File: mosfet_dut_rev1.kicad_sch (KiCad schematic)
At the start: 40 parts, among them J2 Conn, J3 Conn_01x02, J4 Conn_01x02, J5 Conn_01x02, J6 Conn_01x02, J7 USB_C_Receptacle_USB2.0_16P, Q1 AO3400A, Q2 AO3400A, Q3 AO3400A, Q4 AO3400A, U1 AP2112K-3.3, U2 USBLC6-2SC6, U4 INA219AxD, U6 ESP32-WROOM-32E, U7 CH340C

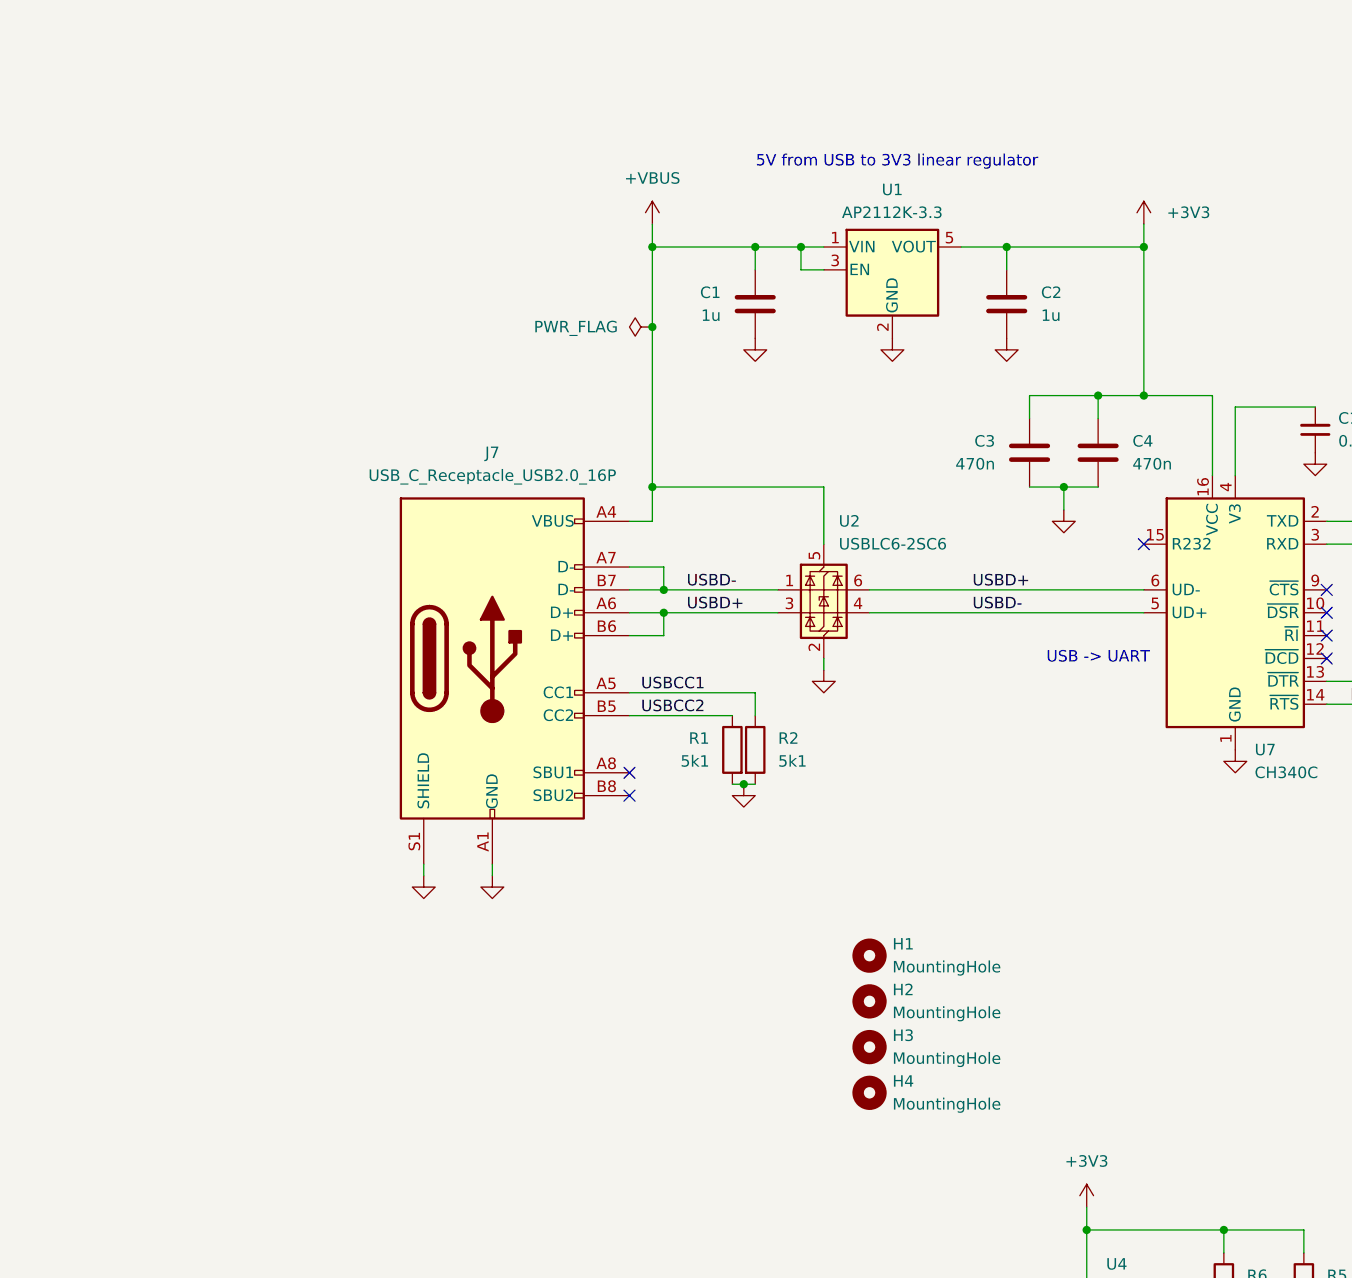
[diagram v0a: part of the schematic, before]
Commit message: Swapping to basic jlcpcb parts APK2112K-3.3 -> ME6211C33M5
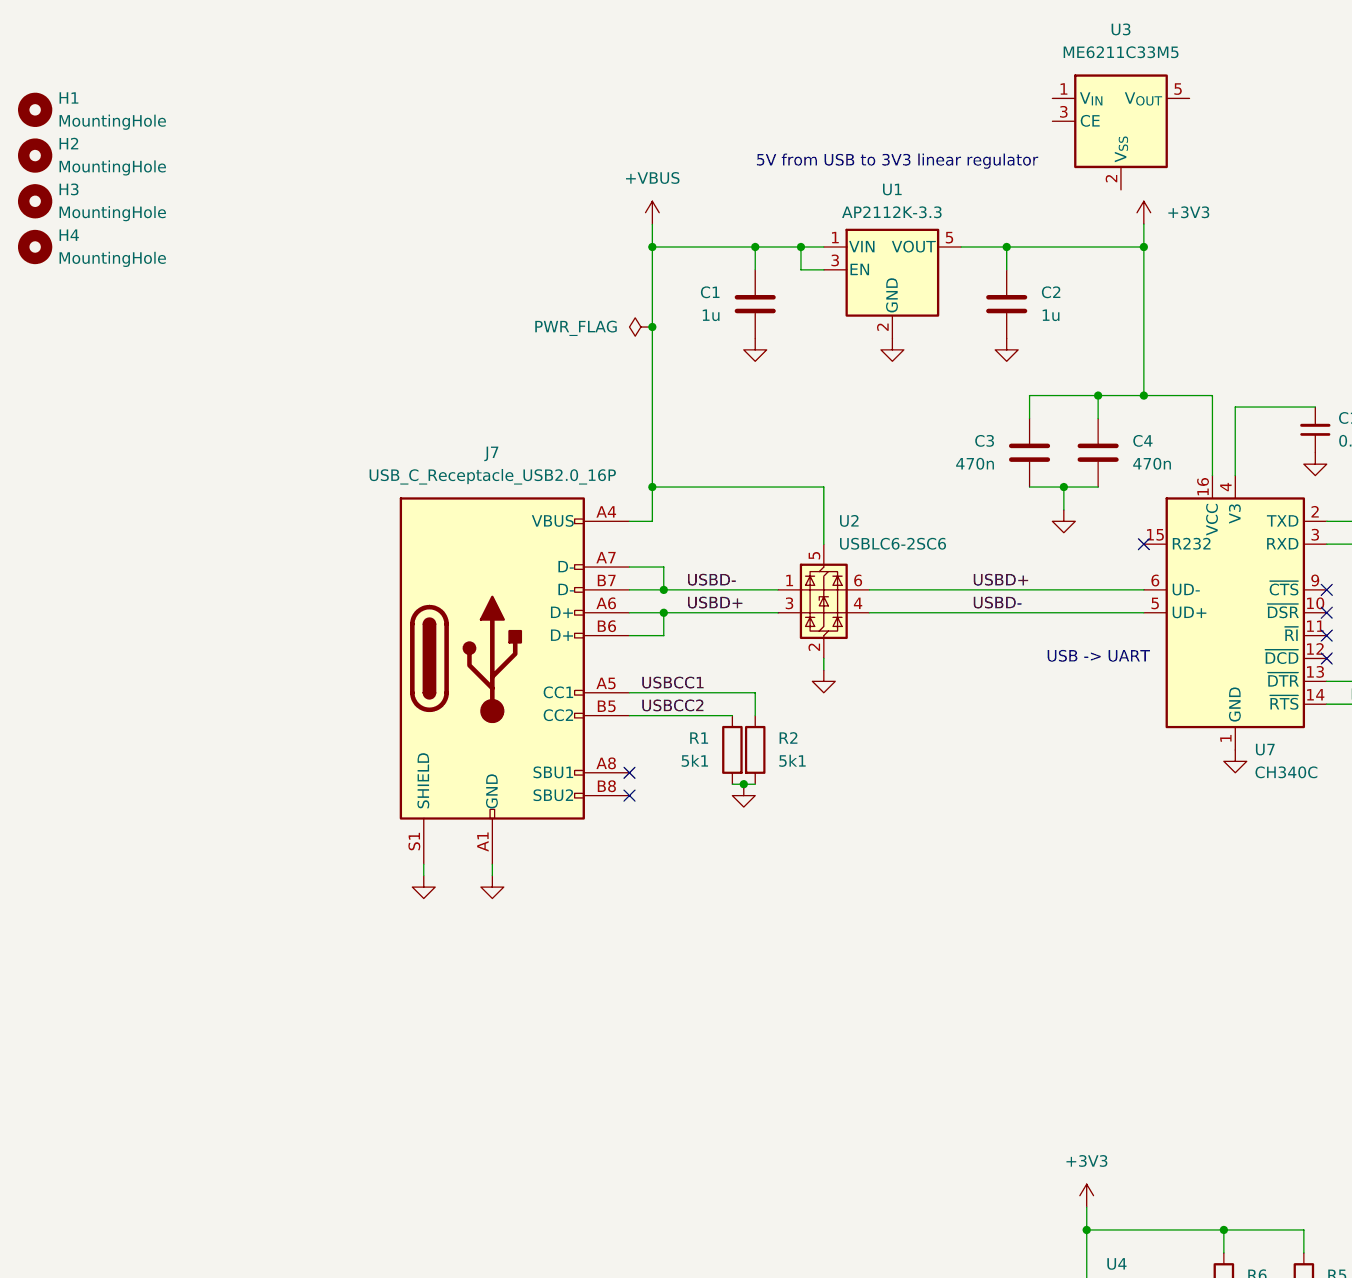
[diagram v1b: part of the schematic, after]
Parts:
- added U3: ME6211C33M5, Package_TO_SOT_SMD:SOT-23-5, symbol Regulator_Linear:ME6211C33M5
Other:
- moved on the sheet: H1, H2, H3, H4
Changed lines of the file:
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@@
 		(title "ESP32 MOSFET DUT")
 		(date "2026-01-06")
-		(rev "1.0")
+		(rev "1.1")
 		(company "Hardware Gunner")
+		(comment 1 "1.1 Swapping to basic jlcpcb parts")
+		(comment 2 "APK2112K-3.3 -> ME6211C33M5")
 	)
 	(text "I2C Addr = 0x40"
@@
 	)
 	(symbol
+		(lib_id "Regulator_Linear:ME6211C33M5")
+		(at 106.68 21.59 0)
+		(unit 1)
+		(exclude_from_sim no)
+		(in_bom yes)
+		(on_board yes)
+		(dnp no)
+		(fields_autoplaced yes)
+		(property "Reference" "U3"
+			(at 106.68 11.43 0)
+			(effects
+				(font
+					(size 1.27 1.27)
+				)
+			)
+		)
+		(property "Value" "ME6211C33M5"
+			(at 106.68 13.97 0)
+			(effects
+				(font
+					(size 1.27 1.27)
+				)
+			)
+		)
+		(property "Footprint" "Package_TO_SOT_SMD:SOT-23-5"
+			(at 106.172 35.052 0)
+			(effects
+				(font
+					(size 1.27 1.27)
+				)
+				(hide yes)
+			)
+		)
+		(property "Datasheet" "https://www.lcsc.com/datasheet/lcsc_datasheet_2304140030_MICRONE-Nanjing-Micro-One-Elec-ME6211C33R5G_C235316.pdf"
+			(at 106.934 38.608 0)
+			(effects
+				(font
+					(size 1.27 1.27)
+				)
+				(hide yes)
+			)
+		)
+		(property "Description" "500mA low dropout linear regulator, shutdown pin, 6.5V max input voltage, 3.3V fixed positive output, SOT-23-5"
+			(at 108.458 36.83 0)
+			(effects
+				(font
+					(size 1.27 1.27)
+				)
+				(hide yes)
+			)
+		)
+		(pin "4"
+		)
+		(pin "3"
+		)
+		(pin "1"
+		)
+		(pin "2"
+		)
+		(pin "5"
+		)
+		(instances
+			(project ""
+				(path "/deac0eab-811f-4736-96ff-e9a031bd3138"
+					(reference "U3")
+					(unit 1)
+				)
+			)
+		)
+	)
+	(symbol
 		(lib_id "power:+3V3")
 		(at 109.22 33.02 0)
@@
 	(symbol
 		(lib_id "Mechanical:MountingHole")
-		(at 78.74 119.38 0)
+		(at -13.97 25.4 0)
 		(unit 1)
 		(exclude_from_sim no)
@@
 		(fields_autoplaced yes)
 		(property "Reference" "H2"
-			(at 81.28 118.1099 0)
+			(at -11.43 24.1299 0)
 			(effects
 				(font
@@
 		)
 		(property "Value" "MountingHole"
-			(at 81.28 120.6499 0)
+			(at -11.43 26.6699 0)
 			(effects
 				(font
@@
 		)
 		(property "Footprint" "MountingHole:MountingHole_3.2mm_M3_Pad"
-			(at 78.74 119.38 0)
+			(at -13.97 25.4 0)
 			(effects
 				(font
@@
 		)
 		(property "Datasheet" "~"
-			(at 78.74 119.38 0)
+			(at -13.97 25.4 0)
 			(effects
 				(font
@@
 		)
 		(property "Description" "Mounting Hole without connection"
-			(at 78.74 119.38 0)
+			(at -13.97 25.4 0)
 			(effects
 				(font
@@
 	(symbol
 		(lib_id "Mechanical:MountingHole")
-		(at 78.74 114.3 0)
+		(at -13.97 20.32 0)
 		(unit 1)
 		(exclude_from_sim no)
@@
 		(fields_autoplaced yes)
 		(property "Reference" "H1"
-			(at 81.28 113.0299 0)
+			(at -11.43 19.0499 0)
 			(effects
 				(font
@@
 		)
 		(property "Value" "MountingHole"
-			(at 81.28 115.5699 0)
+			(at -11.43 21.5899 0)
 			(effects
 				(font
@@
 		)
 		(property "Footprint" "MountingHole:MountingHole_3.2mm_M3_Pad"
-			(at 78.74 114.3 0)
+			(at -13.97 20.32 0)
 			(effects
 				(font
@@
 		)
 		(property "Datasheet" "~"
-			(at 78.74 114.3 0)
+			(at -13.97 20.32 0)
 			(effects
 				(font
@@
 		)
 		(property "Description" "Mounting Hole without connection"
-			(at 78.74 114.3 0)
+			(at -13.97 20.32 0)
 			(effects
 				(font
@@
 	(symbol
 		(lib_id "Mechanical:MountingHole")
-		(at 78.74 124.46 0)
+		(at -13.97 30.48 0)
 		(unit 1)
 		(exclude_from_sim no)
@@
 		(fields_autoplaced yes)
 		(property "Reference" "H3"
-			(at 81.28 123.1899 0)
+			(at -11.43 29.2099 0)
 			(effects
 				(font
@@
 		)
 		(property "Value" "MountingHole"
-			(at 81.28 125.7299 0)
+			(at -11.43 31.7499 0)
 			(effects
 				(font
@@
 		)
 		(property "Footprint" "MountingHole:MountingHole_3.2mm_M3_Pad"
-			(at 78.74 124.46 0)
+			(at -13.97 30.48 0)
 			(effects
 				(font
@@
 		)
 		(property "Datasheet" "~"
-			(at 78.74 124.46 0)
+			(at -13.97 30.48 0)
 			(effects
 				(font
@@
 		)
 		(property "Description" "Mounting Hole without connection"
-			(at 78.74 124.46 0)
+			(at -13.97 30.48 0)
 			(effects
 				(font
@@
 	(symbol
 		(lib_id "Mechanical:MountingHole")
-		(at 78.74 129.54 0)
+		(at -13.97 35.56 0)
 		(unit 1)
 		(exclude_from_sim no)
@@
 		(fields_autoplaced yes)
 		(property "Reference" "H4"
-			(at 81.28 128.2699 0)
+			(at -11.43 34.2899 0)
 			(effects
 				(font
@@
 		)
 		(property "Value" "MountingHole"
-			(at 81.28 130.8099 0)
+			(at -11.43 36.8299 0)
 			(effects
 				(font
@@
 		)
 		(property "Footprint" "MountingHole:MountingHole_3.2mm_M3_Pad"
-			(at 78.74 129.54 0)
+			(at -13.97 35.56 0)
 			(effects
 				(font
@@
 		)
 		(property "Datasheet" "~"
-			(at 78.74 129.54 0)
+			(at -13.97 35.56 0)
 			(effects
 				(font
@@
 		)
 		(property "Description" "Mounting Hole without connection"
-			(at 78.74 129.54 0)
+			(at -13.97 35.56 0)
 			(effects
 				(font

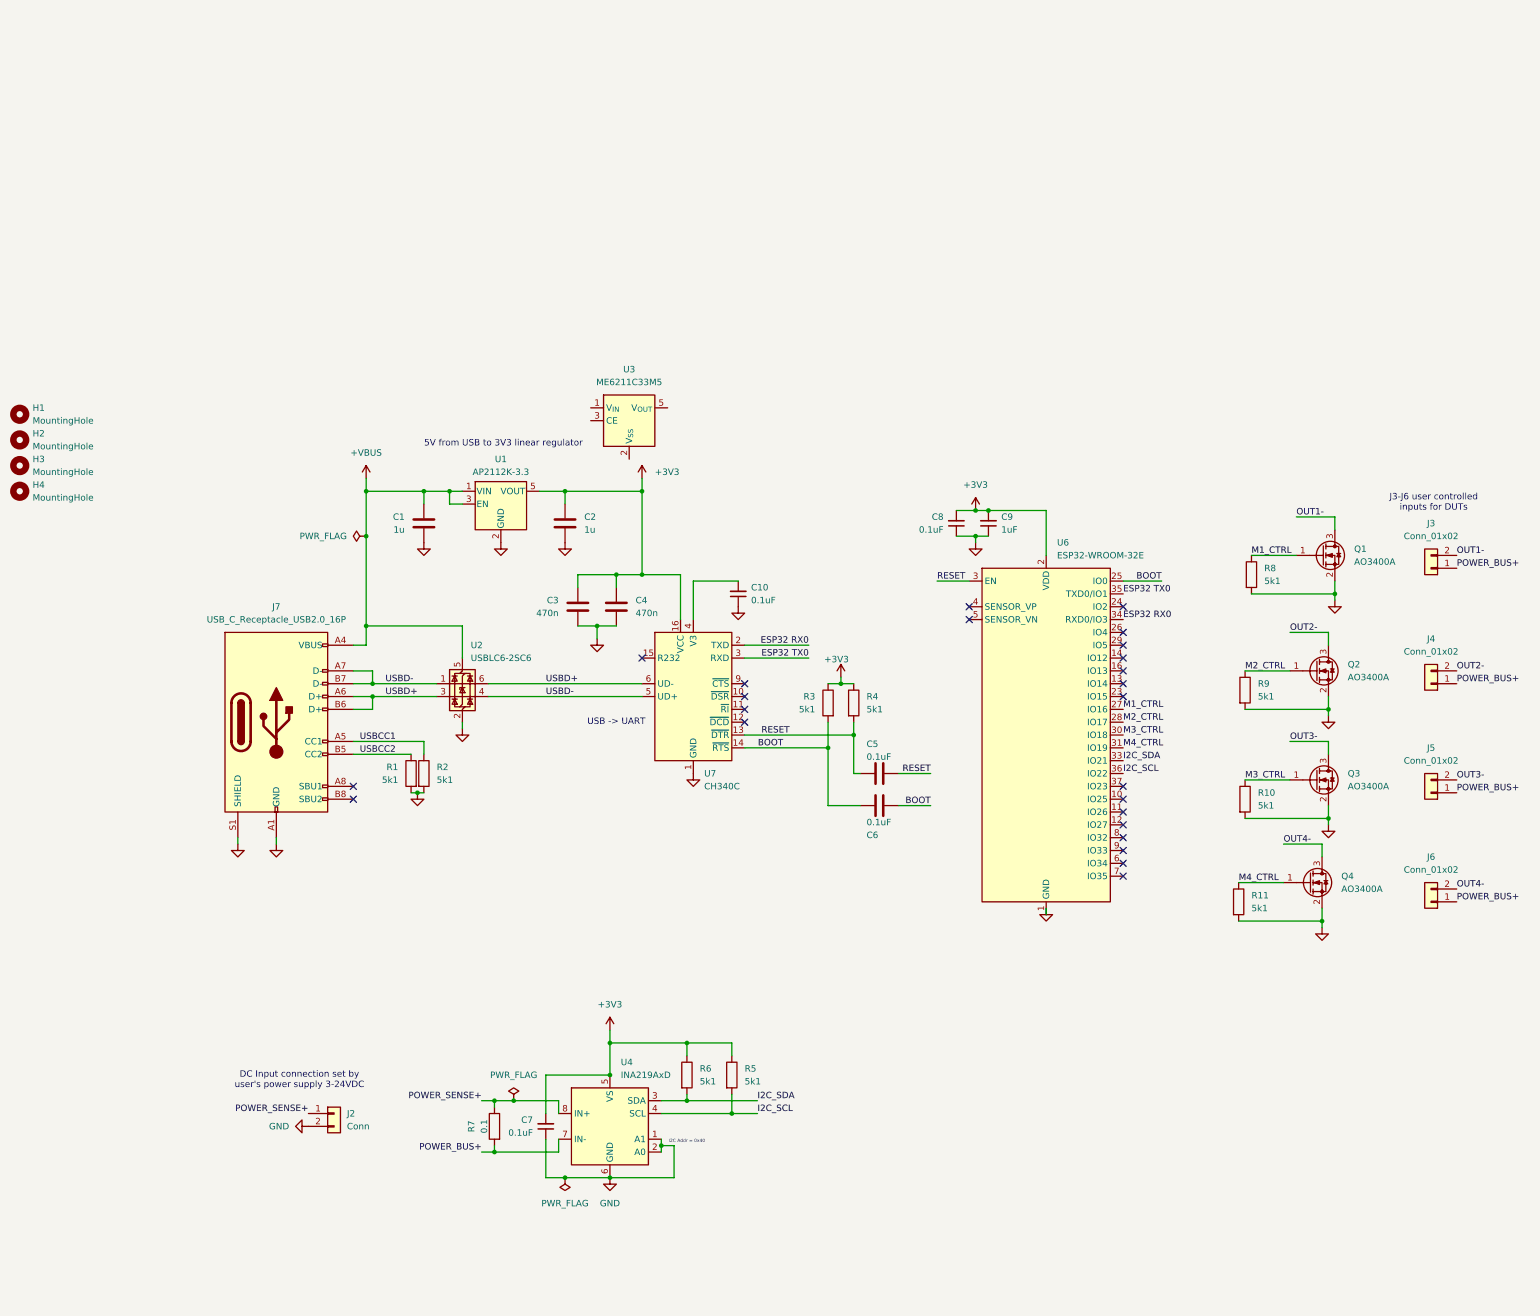
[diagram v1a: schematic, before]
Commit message: MUX/Shunts schematic wiring
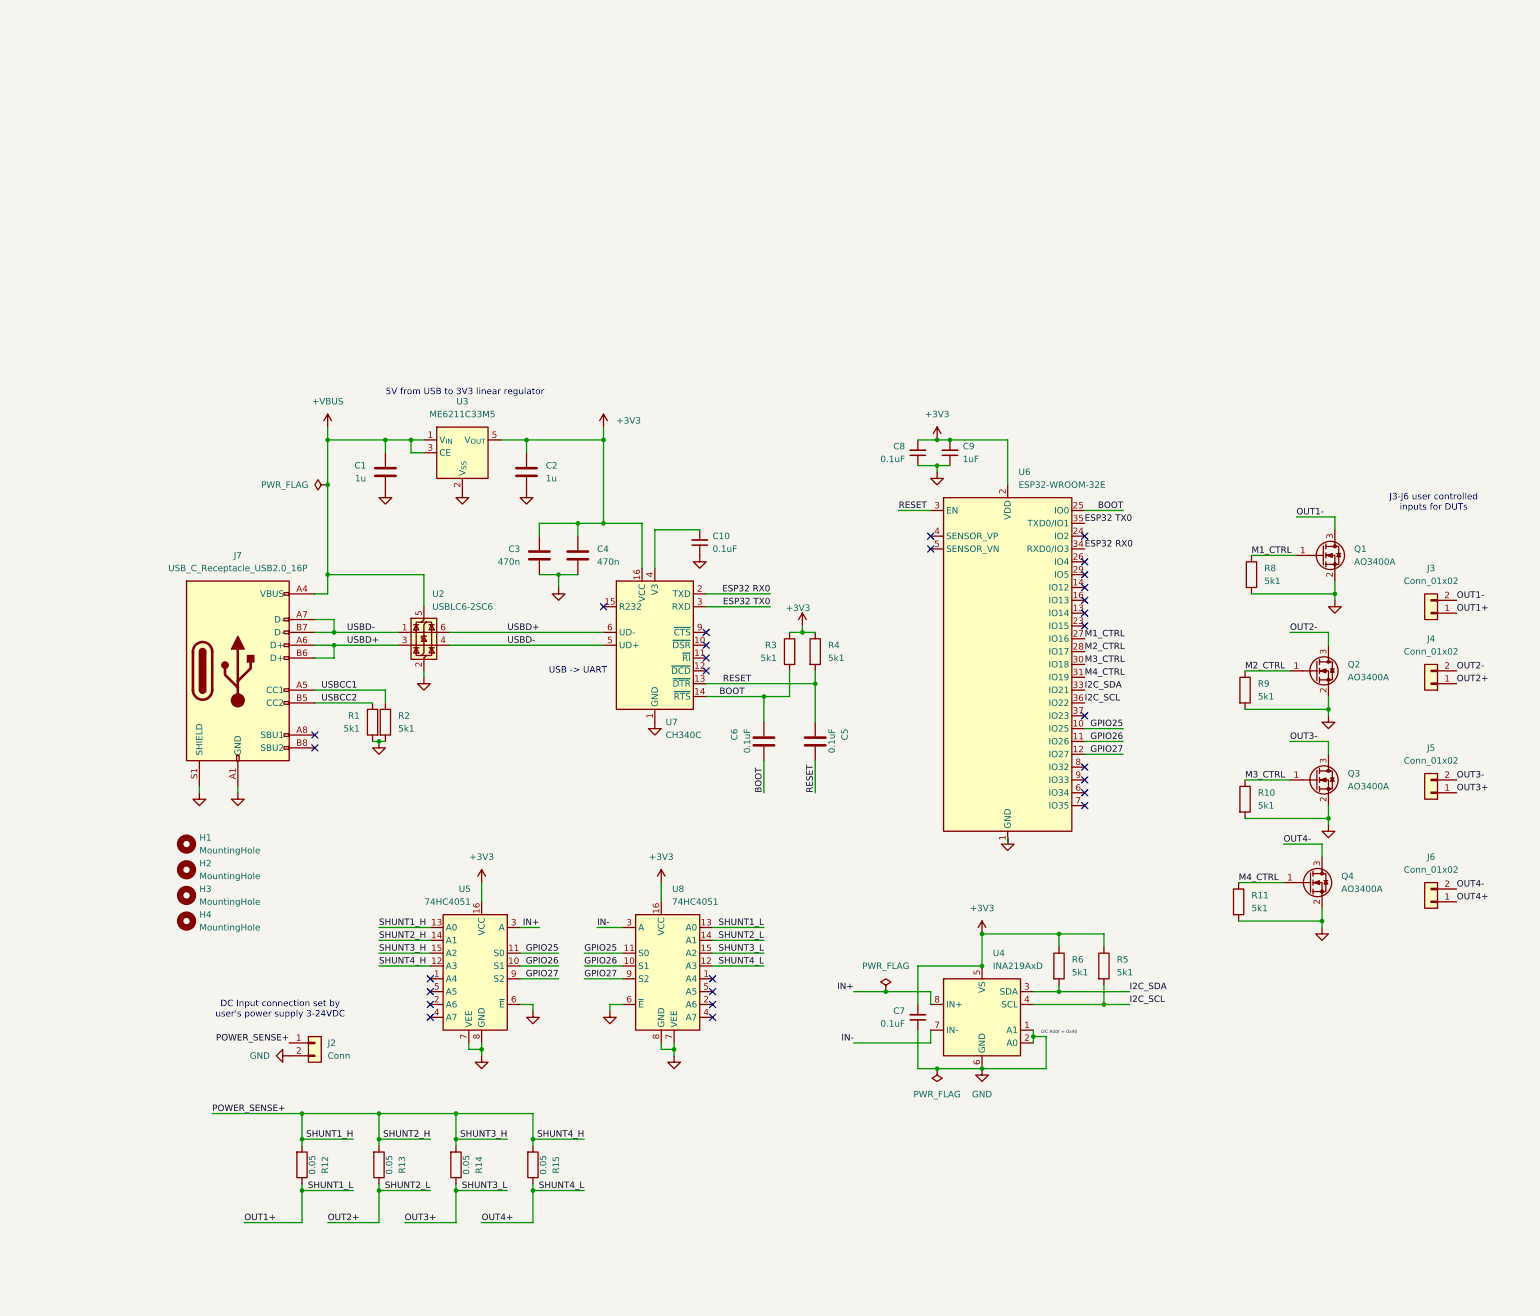
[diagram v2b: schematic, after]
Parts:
- removed R7: 0.1, Resistor_SMD:R_2512_6332Metric, symbol Device:R
- removed U1: AP2112K-3.3, Package_TO_SOT_SMD:SOT-23-5, symbol Regulator_Linear:AP2112K-3.3
- added R12, R13, R14, R15: 0.05, Resistor_SMD:R_2512_6332Metric, symbol Device:R
- added U5, U8: 74HC4051, symbol 74xx:74HC4051
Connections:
- net +3V3: now also U3.5 (V_{OUT}), U5.16 (VCC), U8.16 (VCC)
- net +VBUS: now also U3.1 (V_{IN}), U3.3 (CE)
- net GND: now also U3.2 (V_{SS}), U5.6 (~{E}), U5.7 (VEE), U5.8 (GND), U8.6 (~{E}), U8.7 (VEE), U8.8 (GND)
- net POWER_SENSE+: now also R12.2, R13.2, R14.2, R15.2, U5.12 (A3), U5.13 (A0), U5.14 (A1), U5.15 (A2); no longer U4.8 (IN+)
- net GPIO25: now reaches U6.10 (IO25)
- net GPIO25: now also U5.11 (S0), U8.11 (S0)
- net GPIO26: now reaches U6.11 (IO26)
- net GPIO26: now also U5.10 (S1), U8.10 (S1)
- net GPIO27: now reaches U6.12 (IO27)
- net GPIO27: now also U5.9 (S2), U8.9 (S2)
- removed net POWER_BUS+: J3.1 (Pin_1), J4.1 (Pin_1), J5.1 (Pin_1), J6.1 (Pin_1), U4.7 (IN-)
- new net IN+: U4.8 (IN+), U5.3 (A)
- new net IN-: U4.7 (IN-), U8.3 (A)
- new net OUT1+: J3.1 (Pin_1), R12.1, U8.13 (A0)
- new net OUT2+: J4.1 (Pin_1), R13.1, U8.14 (A1)
- new net OUT3+: J5.1 (Pin_1), R14.1, U8.15 (A2)
- new net OUT4+: J6.1 (Pin_1), R15.1, U8.12 (A3)
- no-connect marks 24 -> 29
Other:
- moved on the sheet: C1, C10, C2, C3, C4, C5, C6, C7, C8, C9, H1, H2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
